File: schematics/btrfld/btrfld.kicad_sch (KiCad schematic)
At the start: 5 parts

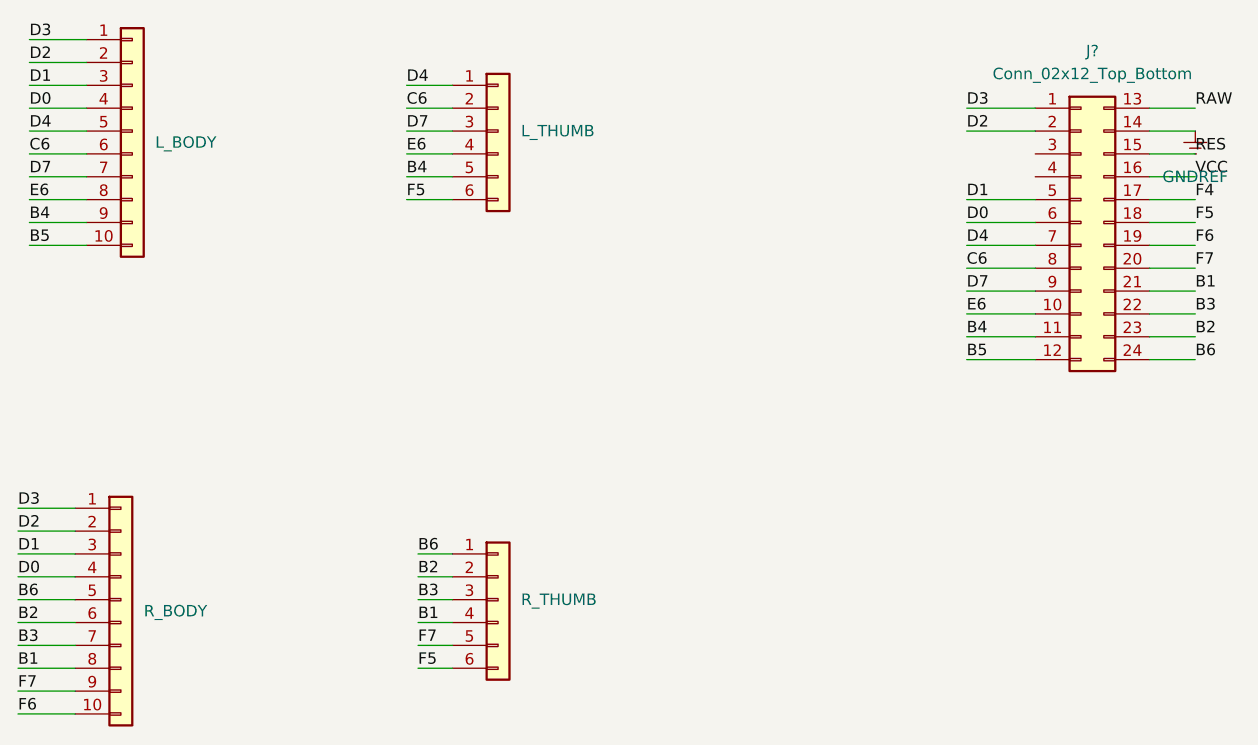
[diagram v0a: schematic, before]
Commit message: major rerouting of cables and swap to elite c
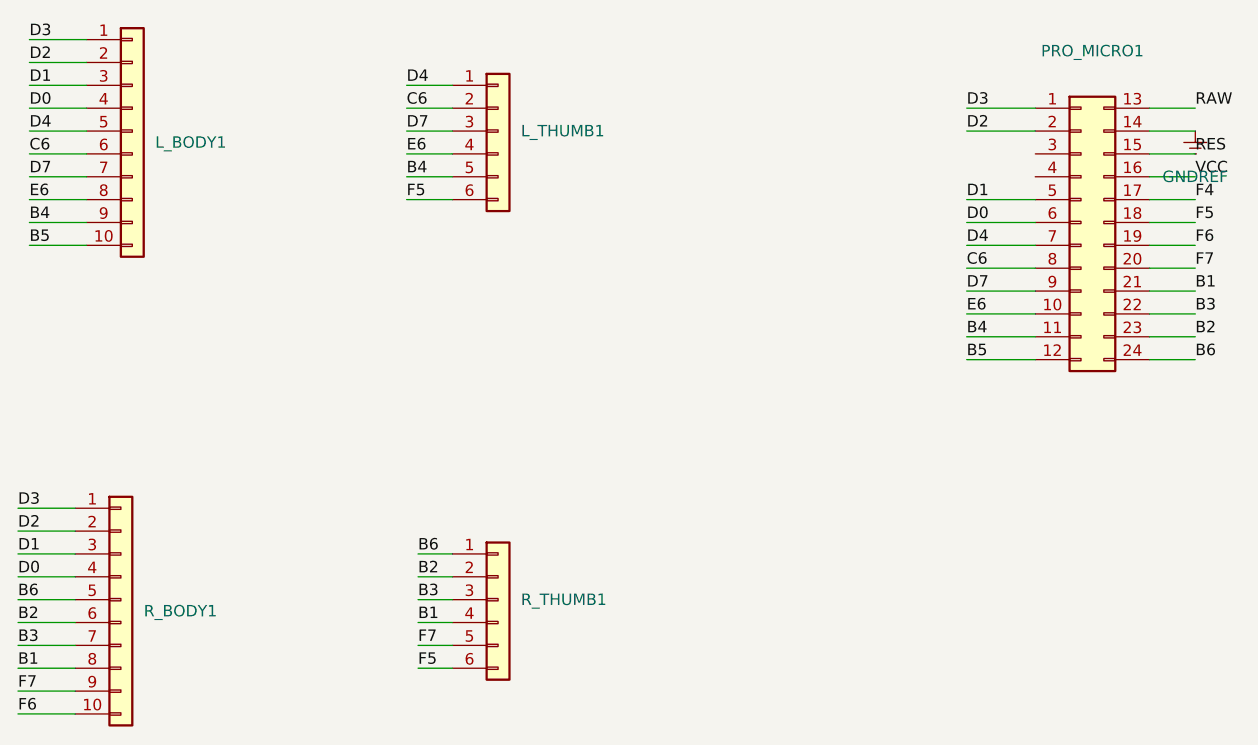
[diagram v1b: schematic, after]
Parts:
- PRO_MICRO1: renamed from J?; footprint (none) -> promicro:ProMicro-EnforcedTop
- renumbered L_BODY to L_BODY1, L_THUMB to L_THUMB1, R_BODY to R_BODY1, R_THUMB to R_THUMB1
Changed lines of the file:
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@@
   (symbol (lib_id "Connector_Generic:Conn_01x06") (at 97.79 64.77 0) (unit 1)
     (in_bom yes) (on_board yes) (fields_autoplaced)
-    (property "Reference" "L_THUMB" (id 0) (at 100.33 64.7699 0)
+    (property "Reference" "L_THUMB1" (id 0) (at 100.33 64.7699 0)
       (effects (font (size 1.27 1.27)) (justify left))
     )
@@
   (symbol (lib_id "Connector_Generic:Conn_01x10") (at 57.15 64.77 0) (unit 1)
     (in_bom yes) (on_board yes) (fields_autoplaced)
-    (property "Reference" "L_BODY" (id 0) (at 59.69 66.0399 0)
+    (property "Reference" "L_BODY1" (id 0) (at 59.69 66.0399 0)
       (effects (font (size 1.27 1.27)) (justify left))
     )
@@
   (symbol (lib_id "Connector_Generic:Conn_01x10") (at 55.88 116.84 0) (unit 1)
     (in_bom yes) (on_board yes) (fields_autoplaced)
-    (property "Reference" "R_BODY" (id 0) (at 58.42 118.1099 0)
+    (property "Reference" "R_BODY1" (id 0) (at 58.42 118.1099 0)
       (effects (font (size 1.27 1.27)) (justify left))
     )
@@
   (symbol (lib_id "Connector_Generic:Conn_02x12_Top_Bottom") (at 162.56 74.93 0) (unit 1)
     (in_bom yes) (on_board yes) (fields_autoplaced)
-    (property "Reference" "J?" (id 0) (at 163.83 55.88 0))
-    (property "Value" "Conn_02x12_Top_Bottom" (id 1) (at 163.83 58.42 0))
-    (property "Footprint" "" (id 2) (at 162.56 74.93 0)
+    (property "Reference" "PRO_MICRO1" (id 0) (at 163.83 55.88 0))
+    (property "Value" "Conn_02x12_Top_Bottom" (id 1) (at 163.83 58.42 0)
+      (effects (font (size 1.27 1.27)) hide)
+    )
+    (property "Footprint" "promicro:ProMicro-EnforcedTop" (id 2) (at 162.56 74.93 0)
       (effects (font (size 1.27 1.27)) hide)
     )
@@
   (symbol (lib_id "power:GNDREF") (at 175.26 64.77 0) (unit 1)
     (in_bom yes) (on_board yes) (fields_autoplaced)
-    (property "Reference" "#PWR?" (id 0) (at 175.26 71.12 0)
+    (property "Reference" "#PWR0101" (id 0) (at 175.26 71.12 0)
       (effects (font (size 1.27 1.27)) hide)
     )
@@
   (symbol (lib_id "Connector_Generic:Conn_01x06") (at 97.79 116.84 0) (unit 1)
     (in_bom yes) (on_board yes) (fields_autoplaced)
-    (property "Reference" "R_THUMB" (id 0) (at 100.33 116.8399 0)
+    (property "Reference" "R_THUMB1" (id 0) (at 100.33 116.8399 0)
       (effects (font (size 1.27 1.27)) (justify left))
     )
@@
   (symbol_instances
     (path "/8001be4c-d1cd-4f03-ad4b-4bb124c07669"
-      (reference "#PWR?") (unit 1) (value "GNDREF") (footprint "")
+      (reference "#PWR0101") (unit 1) (value "GNDREF") (footprint "")
+    )
+    (path "/1021220a-b614-4fcc-97bd-2866f454e6fd"
+      (reference "L_BODY1") (unit 1) (value "Conn_01x10") (footprint "Connector_PinHeader_1.27mm:PinHeader_1x10_P1.27mm_Vertical")
+    )
+    (path "/0e2df8d3-305f-4733-ac80-5dbada55e715"
+      (reference "L_THUMB1") (unit 1) (value "Conn_01x06") (footprint "Connector_PinHeader_1.27mm:PinHeader_1x06_P1.27mm_Vertical")
     )
     (path "/3901f547-5870-4f5a-ac8d-66c6b31ab5c8"
-      (reference "J?") (unit 1) (value "Conn_02x12_Top_Bottom") (footprint "")
-    )
-    (path "/1021220a-b614-4fcc-97bd-2866f454e6fd"
-      (reference "L_BODY") (unit 1) (value "Conn_01x10") (footprint "Connector_PinHeader_1.27mm:PinHeader_1x10_P1.27mm_Vertical")
-    )
-    (path "/0e2df8d3-305f-4733-ac80-5dbada55e715"
-      (reference "L_THUMB") (unit 1) (value "Conn_01x06") (footprint "Connector_PinHeader_1.27mm:PinHeader_1x06_P1.27mm_Vertical")
+      (reference "PRO_MICRO1") (unit 1) (value "Conn_02x12_Top_Bottom") (footprint "promicro:ProMicro-EnforcedTop")
     )
     (path "/28649050-c8c7-4578-8b5e-a0caa49dae82"
-      (reference "R_BODY") (unit 1) (value "Conn_01x10") (footprint "Connector_PinHeader_1.27mm:PinHeader_1x10_P1.27mm_Vertical")
+      (reference "R_BODY1") (unit 1) (value "Conn_01x10") (footprint "Connector_PinHeader_1.27mm:PinHeader_1x10_P1.27mm_Vertical")
     )
     (path "/fd814933-2aea-49b1-9010-53bf9ed6e941"
-      (reference "R_THUMB") (unit 1) (value "Conn_01x06") (footprint "Connector_PinHeader_1.27mm:PinHeader_1x06_P1.27mm_Vertical")
+      (reference "R_THUMB1") (unit 1) (value "Conn_01x06") (footprint "Connector_PinHeader_1.27mm:PinHeader_1x06_P1.27mm_Vertical")
     )
   )
